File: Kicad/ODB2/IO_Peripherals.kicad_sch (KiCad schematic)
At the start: 22 parts, among them J1 USB_B_Micro, J5 RFM_Conn_Coaxial, U10 W25Q512JVEIQ, U4 USBLC6-2P6, U9 RFM22B-433-S2

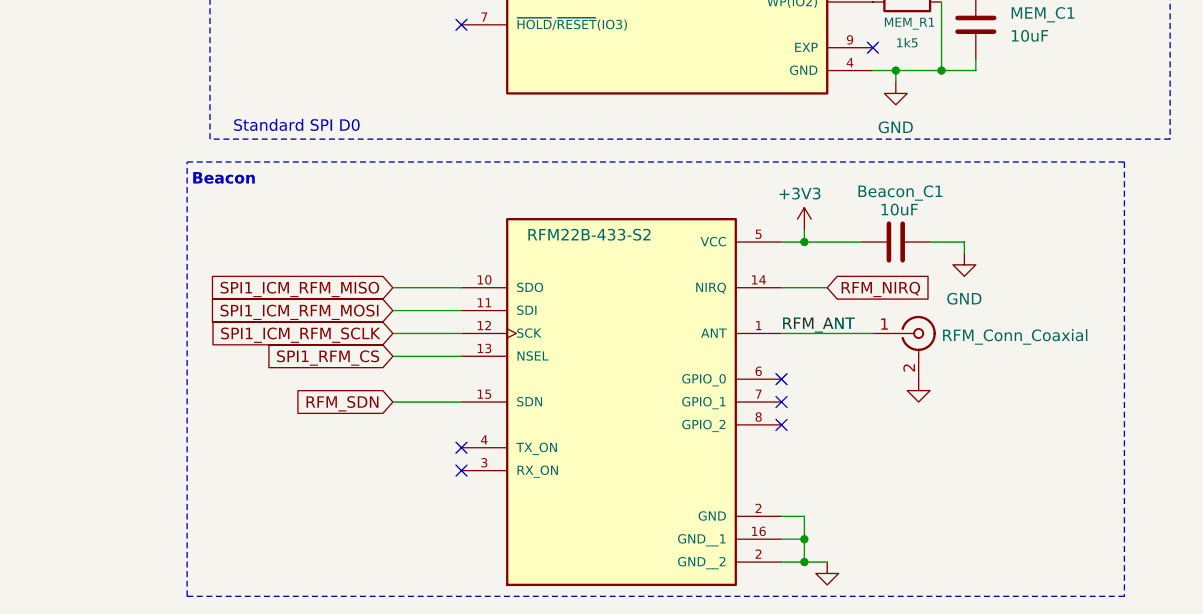
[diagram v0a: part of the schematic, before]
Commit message: fix symbole et footprint rfm22
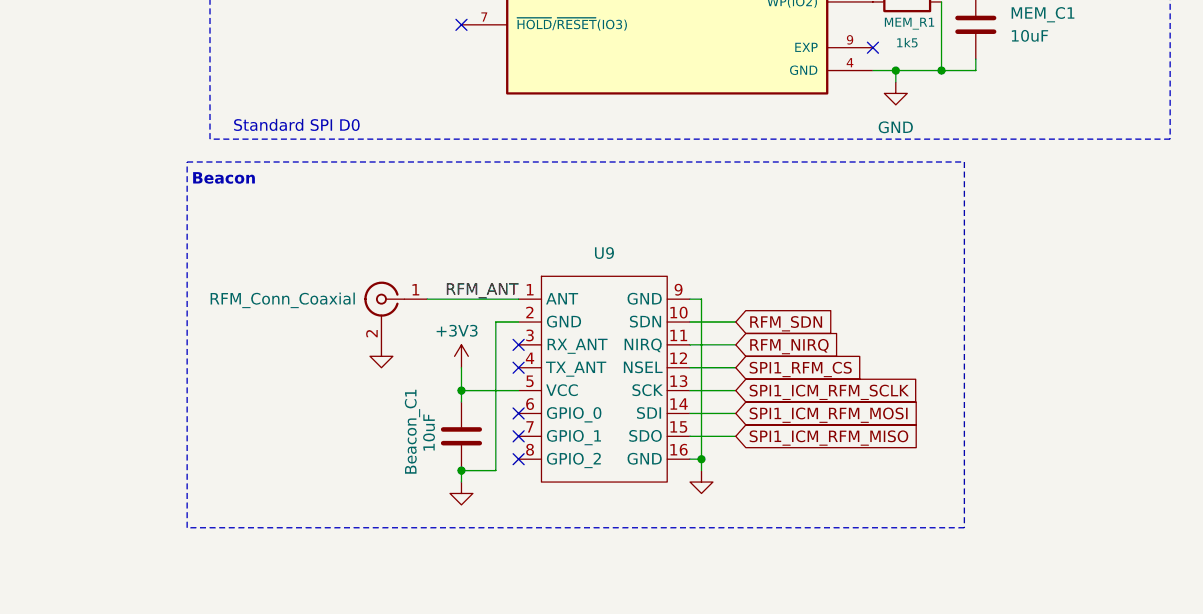
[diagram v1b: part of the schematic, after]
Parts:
- removed U9: RFM22B-433-S2, ODB:RFM22B-433-S2, symbol ODB2:RFM23BP-433-S2
- added U9: ~, ODB:RFM22b-S2, symbol ODB2:RFM22B-S2
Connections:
- net +3V3: now also Beacon_C1.2, U9.5 (VCC); no longer Beacon_C1.1
- net GND: now also Beacon_C1.1, U9.16 (GND), U9.2 (GND), U9.9 (GND); no longer Beacon_C1.2
- net RFM_ANT: now also U9.1 (ANT)
- net RFM_NIRQ: now also U9.11 (NIRQ)
- net RFM_SDN: now also U9.10 (SDN)
- net SPI1_ICM_RFM_MISO: now also U9.15 (SDO)
- net SPI1_ICM_RFM_MOSI: now also U9.14 (SDI)
- net SPI1_ICM_RFM_SCLK: now also U9.13 (SCK)
- net SPI1_RFM_CS: now also U9.12 (NSEL)
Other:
- moved on the sheet: Beacon_C1

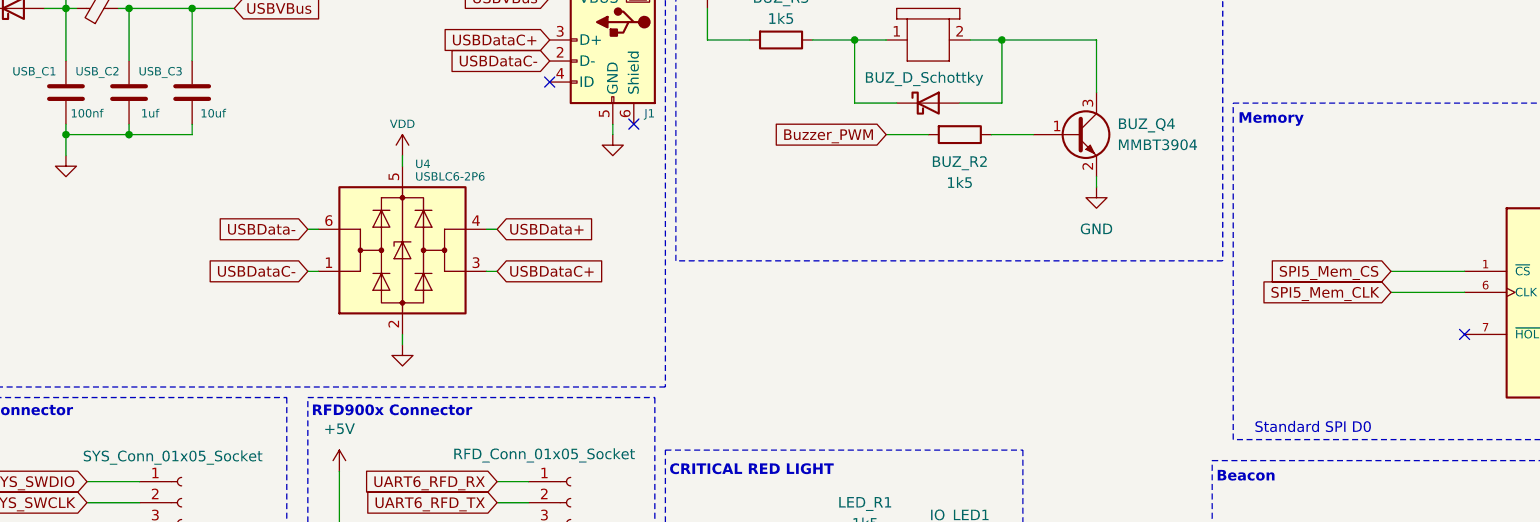
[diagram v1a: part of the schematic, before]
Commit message: Fix labels, 50 ohms, STM no connect
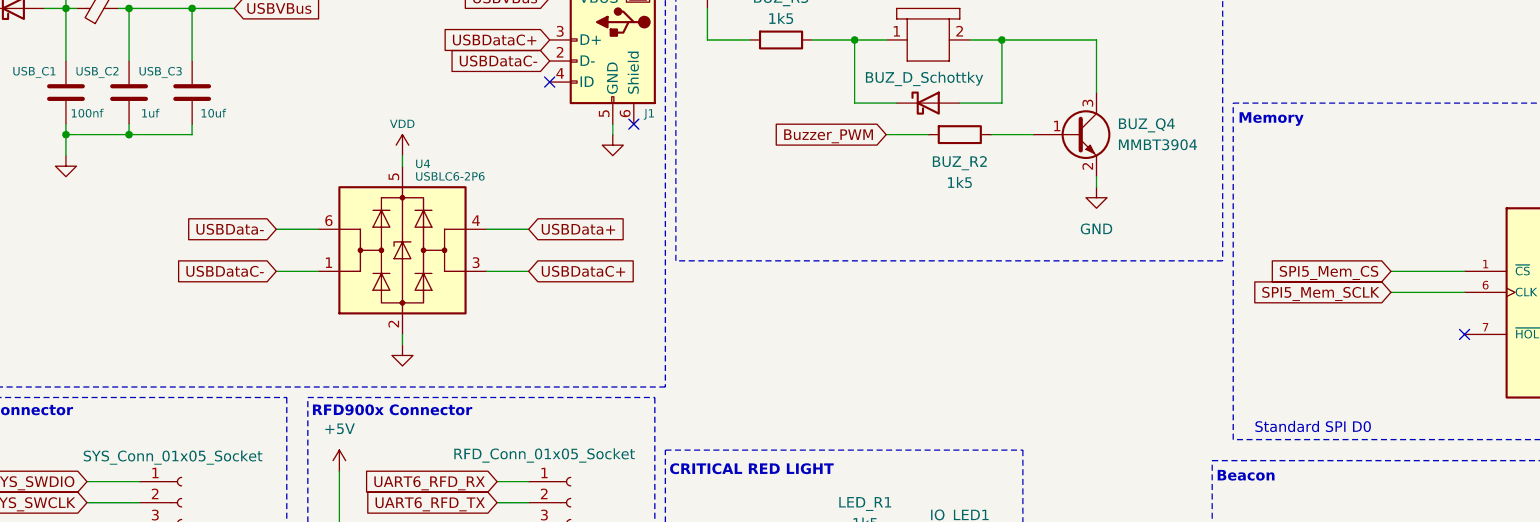
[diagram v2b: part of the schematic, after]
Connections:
- net SPI5_Mem_CLK renamed SPI5_Mem_SCLK
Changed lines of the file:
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@@
 	(wire
 		(pts
-			(xy 82.55 64.77) (xy 83.82 64.77)
+			(xy 82.55 64.77) (xy 87.63 64.77)
 		)
 		(stroke
@@
 	(wire
 		(pts
-			(xy 82.55 59.69) (xy 83.82 59.69)
+			(xy 82.55 59.69) (xy 87.63 59.69)
 		)
 		(stroke
@@
 	(wire
 		(pts
-			(xy 60.96 59.69) (xy 62.23 59.69)
+			(xy 57.15 59.69) (xy 62.23 59.69)
 		)
 		(stroke
@@
 	(wire
 		(pts
-			(xy 60.96 64.77) (xy 62.23 64.77)
+			(xy 57.15 64.77) (xy 62.23 64.77)
 		)
 		(stroke
@@
 	(global_label "USBData+"
 		(shape input)
-		(at 83.82 59.69 0)
+		(at 87.63 59.69 0)
 		(fields_autoplaced yes)
 		(effects
@@
 		)
 		(property "Intersheetrefs" "${INTERSHEET_REFS}"
-			(at 96.4813 59.69 0)
+			(at 100.2913 59.69 0)
 			(effects
 				(font
@@
 	(global_label "USBData-"
 		(shape input)
-		(at 60.96 59.69 180)
+		(at 57.15 59.69 180)
 		(fields_autoplaced yes)
 		(effects
@@
 		)
 		(property "Intersheetrefs" "${INTERSHEET_REFS}"
-			(at 48.2987 59.69 0)
+			(at 44.4887 59.69 0)
 			(effects
 				(font
@@
 		)
 	)
-	(global_label "SPI5_Mem_CLK"
+	(global_label "SPI5_Mem_SCLK"
 		(shape input)
 		(at 191.77 67.31 180)
@@
 		)
 		(property "Intersheetrefs" "${INTERSHEET_REFS}"
-			(at 174.7544 67.31 0)
+			(at 173.5449 67.31 0)
 			(effects
 				(font
@@
 	(global_label "USBDataC+"
 		(shape input)
-		(at 83.82 64.77 0)
+		(at 87.63 64.77 0)
 		(fields_autoplaced yes)
 		(effects
@@
 		)
 		(property "Intersheetrefs" "${INTERSHEET_REFS}"
-			(at 97.7513 64.77 0)
+			(at 101.5613 64.77 0)
 			(effects
 				(font
@@
 	(global_label "USBDataC-"
 		(shape input)
-		(at 60.96 64.77 180)
+		(at 57.15 64.77 180)
 		(fields_autoplaced yes)
 		(effects
@@
 		)
 		(property "Intersheetrefs" "${INTERSHEET_REFS}"
-			(at 47.0287 64.77 0)
+			(at 43.2187 64.77 0)
 			(effects
 				(font
@@
 				(justify left)
 				(hide yes)
+			)
+		)
+	)
+	(netclass_flag ""
+		(length 2.54)
+		(shape round)
+		(at 86.36 64.77 180)
+		(effects
+			(font
+				(size 1.27 1.27)
+			)
+			(justify right bottom)
+		)
+		(property "50 ohm" "50 ohm"
+			(at 83.058 69.342 0)
+			(effects
+				(font
+					(size 1.27 1.27)
+					(italic yes)
+				)
+				(justify left)
+			)
+		)
+	)
+	(netclass_flag ""
+		(length 2.54)
+		(shape round)
+		(at 58.42 64.77 180)
+		(effects
+			(font
+				(size 1.27 1.27)
+			)
+			(justify right bottom)
+		)
+		(property "50 ohm" "50 ohm"
+			(at 55.372 69.342 0)
+			(effects
+				(font
+					(size 1.27 1.27)
+					(italic yes)
+				)
+				(justify left)
 			)
 		)
@@
 			(effects
 				(font
+					(size 1.27 1.27)
+					(italic yes)
+				)
+				(justify left)
+			)
+		)
+	)
+	(netclass_flag ""
+		(length 2.54)
+		(shape round)
+		(at 58.42 59.69 0)
+		(effects
+			(font
+				(size 1.27 1.27)
+			)
+			(justify left bottom)
+		)
+		(property "50 ohm" "50 ohm"
+			(at 56.134 55.372 0)
+			(effects
+				(font
+					(size 1.27 1.27)
+					(italic yes)
+				)
+				(justify left)
+			)
+		)
+	)
+	(netclass_flag ""
+		(length 2.54)
+		(shape round)
+		(at 86.36 59.69 0)
+		(effects
+			(font
+				(size 1.27 1.27)
+			)
+			(justify left bottom)
+		)
+		(property "50 ohm" "50 ohm"
+			(at 84.074 55.372 0)
+			(effects
+				(font

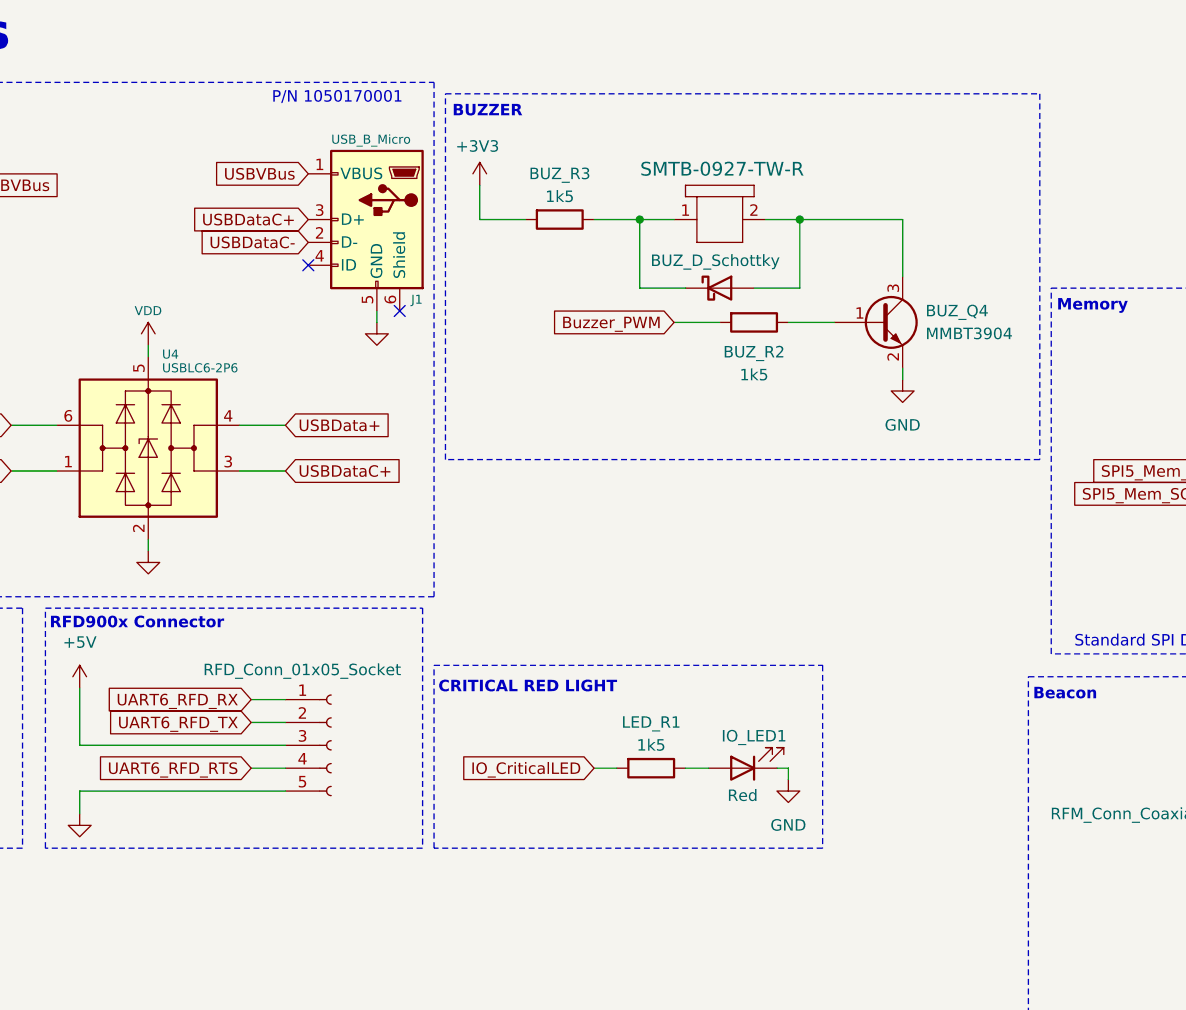
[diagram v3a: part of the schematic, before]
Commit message: fix Labels + fix STM32 projet pinout
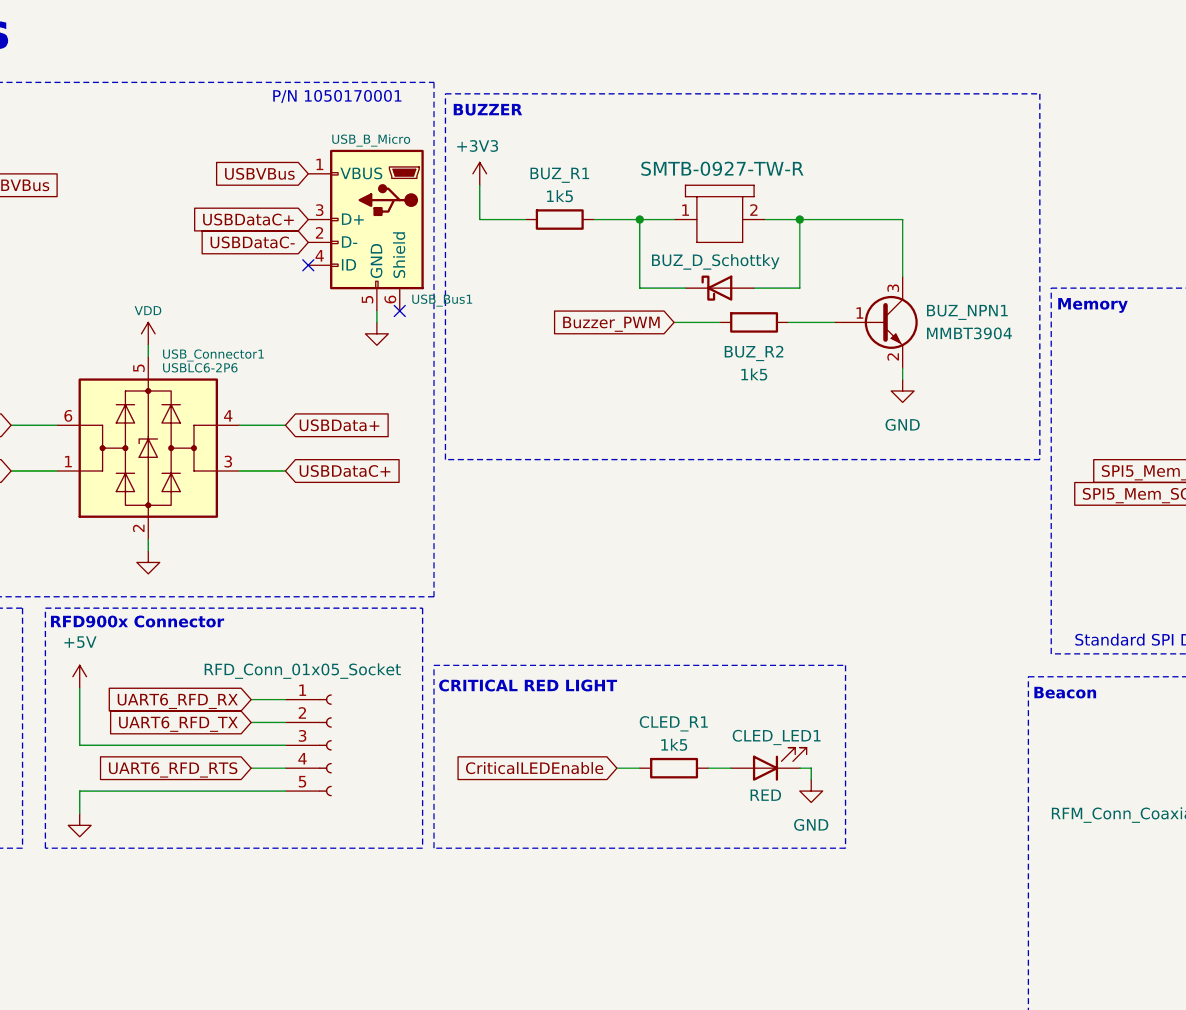
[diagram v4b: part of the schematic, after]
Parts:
- CLED_LED1: renamed from IO_LED1; value Red -> RED
- renumbered LS1 to BUZ_Buzzer1, BUZ_Q4 to BUZ_NPN1, BUZ_R3 to BUZ_R1, LED_R1 to CLED_R1, J1 to USB_Bus1, U4 to USB_Connector1
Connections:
- net IO_CriticalLED renamed CriticalLEDEnable
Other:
- moved on the sheet: CLED_LED1, CLED_R1
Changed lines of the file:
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@@
 	(wire
 		(pts
-			(xy 142.24 97.79) (xy 143.51 97.79)
+			(xy 144.78 97.79) (xy 146.05 97.79)
 		)
 		(stroke
@@
 	(wire
 		(pts
-			(xy 132.08 97.79) (xy 134.62 97.79)
+			(xy 134.62 97.79) (xy 137.16 97.79)
 		)
 		(stroke
@@
 	(wire
 		(pts
-			(xy 143.51 97.79) (xy 143.51 99.06)
+			(xy 146.05 97.79) (xy 146.05 99.06)
 		)
 		(stroke
@@
 	(wire
 		(pts
-			(xy 121.92 97.79) (xy 124.46 97.79)
+			(xy 124.46 97.79) (xy 127 97.79)
 		)
 		(stroke
@@
 	(rectangle
 		(start 104.14 86.36)
-		(end 147.32 106.68)
+		(end 149.86 106.68)
 		(stroke
 			(width 0)
@@
 		)
 	)
-	(global_label "IO_CriticalLED"
+	(global_label "CriticalLEDEnable"
 		(shape input)
-		(at 121.92 97.79 180)
+		(at 124.46 97.79 180)
 		(fields_autoplaced yes)
 		(effects
@@
 		)
 		(property "Intersheetrefs" "${INTERSHEET_REFS}"
-			(at 105.6905 97.79 0)
+			(at 104.7836 97.79 0)
 			(effects
 				(font
@@
 	(symbol
 		(lib_id "Device:LED")
-		(at 138.43 97.79 180)
+		(at 140.97 97.79 180)
 		(unit 1)
 		(exclude_from_sim no)
@@
 		(on_board yes)
 		(dnp no)
-		(property "Reference" "IO_LED1"
-			(at 139.7 94.234 0)
+		(property "Reference" "CLED_LED1"
+			(at 142.24 94.234 0)
 			(effects
 				(font
@@
 			)
 		)
-		(property "Value" "Red"
-			(at 138.43 100.838 0)
+		(property "Value" "RED"
+			(at 140.97 100.838 0)
 			(effects
 				(font
@@
 		)
 		(property "Footprint" "LED_SMD:LED_0805_2012Metric"
-			(at 138.43 97.79 0)
+			(at 140.97 97.79 0)
 			(effects
 				(font
@@
 		)
 		(property "Datasheet" "~"
-			(at 138.43 97.79 0)
+			(at 140.97 97.79 0)
 			(effects
 				(font
@@
 		)
 		(property "Description" "Light emitting diode"
-			(at 138.43 97.79 0)
+			(at 140.97 97.79 0)
 			(effects
 				(font
@@
 			(project "ODB2"
 				(path "/4b06c5d1-aa8b-48ed-8972-b43a60cfab78/93865dc8-71fa-4dc6-90ce-f5a9779dfd41"
-					(reference "IO_LED1")
+					(reference "CLED_LED1")
 					(unit 1)
 				)
@@
 		(dnp no)
 		(fields_autoplaced yes)
-		(property "Reference" "BUZ_Q4"
+		(property "Reference" "BUZ_NPN1"
 			(at 158.75 46.9899 0)
 			(effects
@@
 			(project ""
 				(path "/4b06c5d1-aa8b-48ed-8972-b43a60cfab78/93865dc8-71fa-4dc6-90ce-f5a9779dfd41"
-					(reference "BUZ_Q4")
+					(reference "BUZ_NPN1")
 					(unit 1)
 				)
@@
 		(on_board yes)
 		(dnp no)
-		(property "Reference" "BUZ_R3"
+		(property "Reference" "BUZ_R1"
 			(at 118.11 31.75 90)
 			(effects
@@
 			(project ""
 				(path "/4b06c5d1-aa8b-48ed-8972-b43a60cfab78/93865dc8-71fa-4dc6-90ce-f5a9779dfd41"
-					(reference "BUZ_R3")
+					(reference "BUZ_R1")
 					(unit 1)
 				)
@@
 		(on_board yes)
 		(dnp no)
-		(property "Reference" "U4"
+		(property "Reference" "USB_Connector1"
 			(at 73.914 51.816 0)
 			(effects
@@
 			(project "ODB2"
 				(path "/4b06c5d1-aa8b-48ed-8972-b43a60cfab78/93865dc8-71fa-4dc6-90ce-f5a9779dfd41"
-					(reference "U4")
+					(reference "USB_Connector1")
 					(unit 1)
 				)
@@
 	(symbol
 		(lib_id "Device:R")
-		(at 128.27 97.79 270)
+		(at 130.81 97.79 270)
 		(unit 1)
 		(exclude_from_sim no)
@@
 		(on_board yes)
 		(dnp no)
-		(property "Reference" "LED_R1"
-			(at 128.27 92.71 90)
+		(property "Reference" "CLED_R1"
+			(at 130.81 92.71 90)
 			(effects
 				(font
@@
 		)
 		(property "Value" "1k5"
-			(at 128.27 95.25 90)
+			(at 130.81 95.25 90)
 			(effects
 				(font
@@
 		)
 		(property "Footprint" "Resistor_SMD:R_0805_2012Metric"
-			(at 128.27 96.012 90)
+			(at 130.81 96.012 90)
 			(effects
 				(font
@@
 		)
 		(property "Datasheet" "~"
-			(at 128.27 97.79 0)
+			(at 130.81 97.79 0)
 			(effects
 				(font
@@
 		)
 		(property "Description" "Resistor"
-			(at 128.27 97.79 0)
+			(at 130.81 97.79 0)
 			(effects
 				(font
@@
 			(project "ODB2"
 				(path "/4b06c5d1-aa8b-48ed-8972-b43a60cfab78/93865dc8-71fa-4dc6-90ce-f5a9779dfd41"
-					(reference "LED_R1")
+					(reference "CLED_R1")
 					(unit 1)
 				)
@@
 		(on_board yes)
 		(dnp no)
-		(property "Reference" "J1"
+		(property "Reference" "USB_Bus1"
 			(at 101.6 45.72 0)
 			(effects
@@
 			(project "ODB2"
 				(path "/4b06c5d1-aa8b-48ed-8972-b43a60cfab78/93865dc8-71fa-4dc6-90ce-f5a9779dfd41"
-					(reference "J1")
+					(reference "USB_Bus1")
 					(unit 1)
 				)
@@
 	(symbol
 		(lib_id "power:GND")
-		(at 143.51 99.06 0)
+		(at 146.05 99.06 0)
 		(unit 1)
 		(exclude_from_sim no)
@@
 		(fields_autoplaced yes)
 		(property "Reference" "#PWR091"
-			(at 143.51 105.41 0)
+			(at 146.05 105.41 0)
 			(effects
 				(font
@@
 		)
 		(property "Value" "GND"
-			(at 143.51 104.14 0)
+			(at 146.05 104.14 0)
 			(effects
 				(font
@@
 		)
 		(property "Footprint" ""
-			(at 143.51 99.06 0)
+			(at 146.05 99.06 0)
 			(effects
 				(font
@@
 		)
 		(property "Datasheet" ""
-			(at 143.51 99.06 0)
+			(at 146.05 99.06 0)
 			(effects
 				(font
@@
 		)
 		(property "Description" "Power symbol creates a global label with name \"GND\" , ground"
-			(at 143.51 99.06 0)
+			(at 146.05 99.06 0)
 			(effects
 				(font
@@
 		(on_board yes)
 		(dnp no)
-		(property "Reference" "LS1"
+		(property "Reference" "BUZ_Buzzer1"
 			(at 135.89 26.67 0)
 			(effects
@@
 			(project ""
 				(path "/4b06c5d1-aa8b-48ed-8972-b43a60cfab78/93865dc8-71fa-4dc6-90ce-f5a9779dfd41"
-					(reference "LS1")
+					(reference "BUZ_Buzzer1")
 					(unit 1)
 				)

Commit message: Fix somes issue
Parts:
- BUZ_R1, BUZ_R2, CLED_R1, MEM_R1: footprint Resistor_SMD:R_0805_2012Metric -> Resistor_SMD:R_0603_1608Metric
- Beacon_C1, MEM_C1, USB_C1, USB_C2, USB_C3: footprint Capacitor_SMD:C_0805_2012Metric -> Capacitor_SMD:C_0603_1608Metric
- CLED_LED1: footprint LED_SMD:LED_0805_2012Metric -> LED_SMD:LED_0603_1608Metric
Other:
- moved on the sheet: BUZ_NPN1, BUZ_R1, BUZ_R2, Beacon_C1, CLED_LED1, CLED_R1, MEM_C1, MEM_R1, U9
